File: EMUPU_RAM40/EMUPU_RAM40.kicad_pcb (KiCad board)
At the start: 2 copper layers, 99.1 x 85.2 mm, 29 parts, among them J1 Conn_01x20_Socket, J2 Conn_01x20_Socket, J3 Barrel_Jack_Switch, J4 Conn_01x06_Pin, J5 Conn_01x08_Pin, J7 PinHeader_1x06_P2.54mm_Vertic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, SW1 SW_SPDT, SW2 SW_SPST, U1 PIC18F47Q43-IP, U2 628128

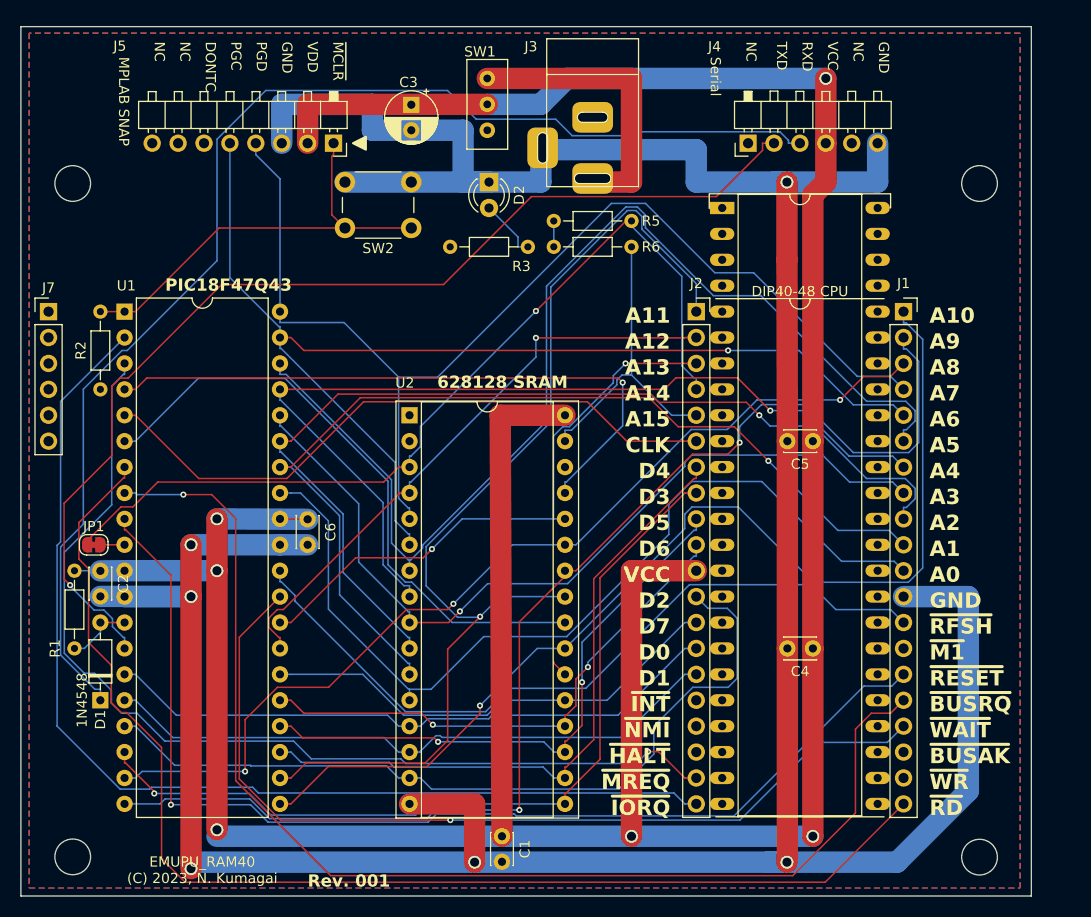
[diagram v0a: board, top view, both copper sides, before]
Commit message: under construction for Rev003 done the follows * fix PowerPlug pin assignment * change /MREQ, /RD, /WR for full_direct * A jumper is assigned to SRAM CS2 (now pulled-up) * add jumpers on /MREQ, /RD, /WR * /INT, /M1 connection to RB5 and RA4. * cut a wire between PB5 and A13, * add pull-down resistors to A13 * add pull up resistors to /MREQ, /RD and /WR.
remains for the following
* add TEST pin
* add LEDs and resistors, including RESET, BUSACK, and HALT
* add pull down resistors to A15-A8, as needed.* add some jumpers for SDcard controls (A9-A12)
* add four jumpers for SDcard (A9-A12)

After confirming 8byte rewrite and reset bootloading, I will finishes the remains.
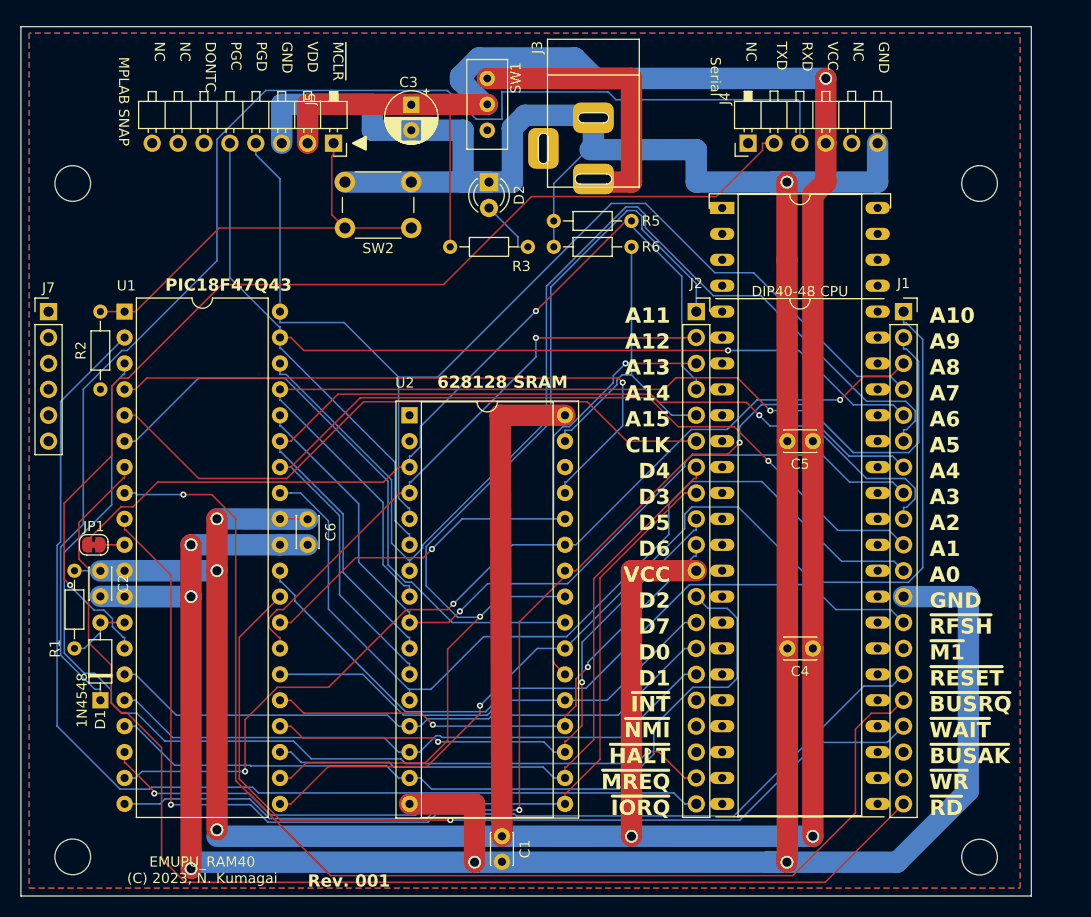
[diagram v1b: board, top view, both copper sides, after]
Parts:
- J3: footprint 0-local:BARREL_JACK -> 0-Project:BARREL_JACK
- J4: footprint 0-local:PinHeader_1x06_P2.54mm_Horizontal_NoFeet -> 0-Project:PinHeader_1x06_P2.54mm_Horizontal_NoFeet
- J5: footprint 0-local:PinHeader_1x08_P2.54mm_Rev_Horizontal_Nofoot -> 0-Project:PinHeader_1x08_P2.54mm_Rev_Horizontal_Nofoot
- SW1: footprint 0-local:PowerSW_for_SBC_series -> 0-Project:PowerSW_for_SBC_series
- SW2: footprint 0-local:SW_PUSH_6mm_H4.3mm -> 0-Project:SW_PUSH_6mm_H4.3mm
- moved J3 0.09 mm to (146.1, 75.0)
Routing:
- net VCC: track 326.7 -> 348.0 mm
- net GND: track 341.8 -> 356.5 mm
- net Net-(D1-K): track 125.3 -> 131.1 mm

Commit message: Rev003: arrange new footprints, before autorouting
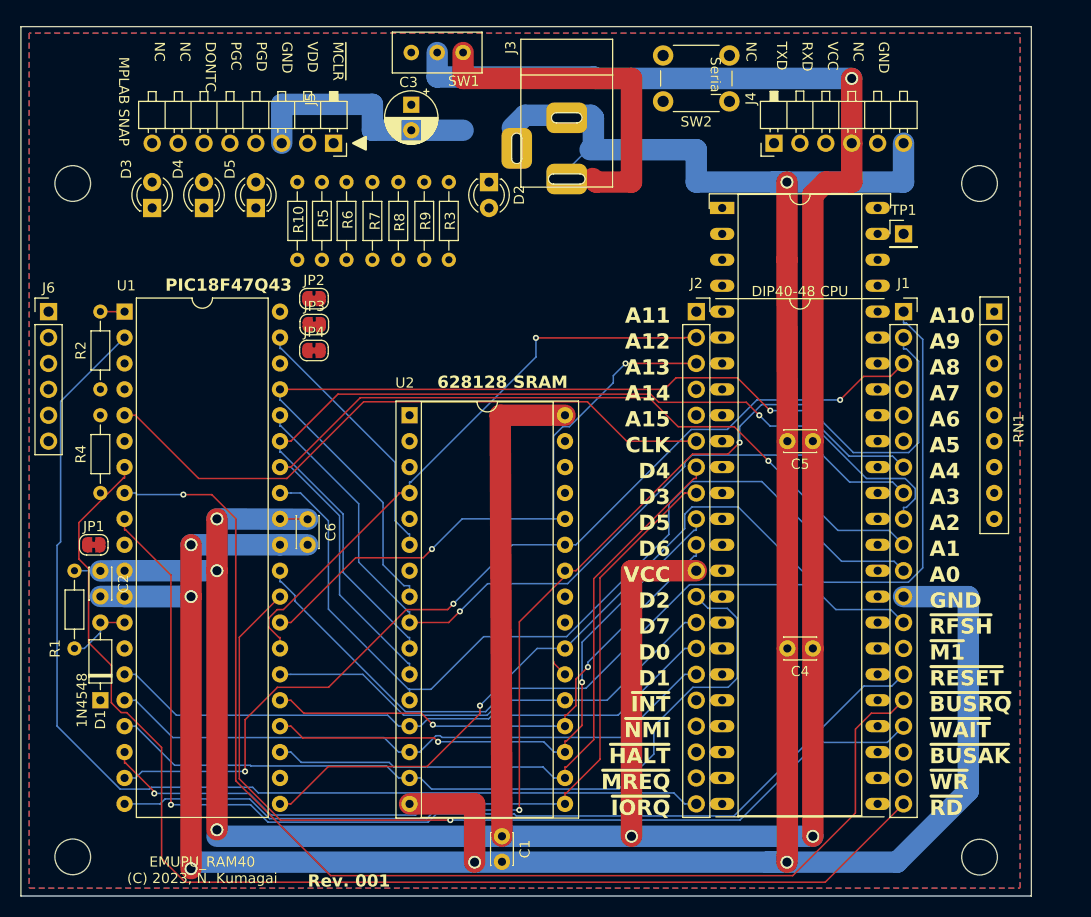
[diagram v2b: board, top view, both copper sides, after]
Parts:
- removed J7: PinHeader_1x06_P2.54mm_Vertical, Connector_PinHeader_2.54mm:PinHeader_1x06_P2.54mm_Vertical
- added D3: BUSAK, LED_THT:LED_D3.0mm, F.Cu at (102.9, 83.8)
- added D4: RESET, LED_THT:LED_D3.0mm, F.Cu at (108.0, 83.8)
- added D5: HALT, LED_THT:LED_D3.0mm, F.Cu at (113.0, 83.8)
- added J6: Conn_01x06_Pin, Connector_PinHeader_2.54mm:PinHeader_1x06_P2.54mm_Vertical, F.Cu at (92.7, 94.0)
- added JP2: SolderJumper_2_Bridged, Jumper:SolderJumper-2_P1.3mm_Bridged_RoundedPad1.0x1.5mm, F.Cu at (118.7, 92.7)
- added JP3: SolderJumper_2_Bridged, Jumper:SolderJumper-2_P1.3mm_Bridged_RoundedPad1.0x1.5mm, F.Cu at (118.8, 95.2)
- added JP4: SolderJumper_2_Bridged, Jumper:SolderJumper-2_P1.3mm_Bridged_RoundedPad1.0x1.5mm, F.Cu at (118.7, 97.8)
- added R10: 1.5k, Resistor_THT:R_Axial_DIN0204_L3.6mm_D1.6mm_P7.62mm_Horizontal, F.Cu at (117.1, 81.3)
- added R4: 10k, Resistor_THT:R_Axial_DIN0204_L3.6mm_D1.6mm_P7.62mm_Horizontal, F.Cu at (97.8, 111.8)
- added R7: 10k, Resistor_THT:R_Axial_DIN0204_L3.6mm_D1.6mm_P7.62mm_Horizontal, F.Cu at (124.5, 81.3)
- added R8: 10k, Resistor_THT:R_Axial_DIN0204_L3.6mm_D1.6mm_P7.62mm_Horizontal, F.Cu at (127.0, 81.3)
- added R9: 10k, Resistor_THT:R_Axial_DIN0204_L3.6mm_D1.6mm_P7.62mm_Horizontal, F.Cu at (129.5, 81.3)
- added RN1: R_Network08, Resistor_THT:R_Array_SIP9, F.Cu at (185.4, 94.0)
- added TP1: TEST, Connector_PinHeader_2.54mm:PinHeader_1x01_P2.54mm_Vertical, F.Cu at (176.5, 86.4)
- R5, R6: value 10k -> 1.5k
- moved SW2 33.6 mm to (159.5, 73.4)
- moved R5 30.6 mm to (119.5, 81.3), turned to -90 degrees
- moved R6 28.7 mm to (121.9, 81.3), turned to -90 degrees
- moved SW1 7.07 mm to (130.8, 68.6), turned to 180 degrees
- moved R3 6.35 mm to (132.0, 81.3), turned to -90 degrees
- moved J3 2.61 mm to (143.5, 75.0)
- moved J4 2.54 mm to (163.8, 77.5)
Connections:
- J2 pad 1: /A11 -> Net-(J2-Pin_1)
- J2 pad 2: /A12 -> Net-(J2-Pin_2)
- J2 pad 3: /A13 -> Net-(J2-Pin_3)
- J2 pad 4: /A14 -> Net-(J2-Pin_4)
- J2 pad 5: /A15 -> Net-(J2-Pin_5)
- JP1 pad 1: /A14 -> Net-(JP1-A)
- JP1 pad 2: Net-(JP1-B) -> VCC
- R5 pad 1: /A14 -> VCC
- R5 pad 2: GND -> Net-(D3-A)
- R6 pad 1: /A15 -> VCC
- R6 pad 2: GND -> Net-(D4-A)
- U1 pad 10: Net-(JP1-B) -> /TEST
- U1 pad 19: /A8 -> /SCLK
- U1 pad 20: /A9 -> /MISO
- U1 pad 21: /A10 -> /MOSI
- U1 pad 22: /A11 -> /SS
- U1 pad 27: /A12 -> unconnected-(U1-RD4-Pad27)
- U1 pad 28: /A13 -> /~{INT}
- U1 pad 6: Net-(U1-RA4) -> /~{M1}
- U1 pad 7: /~{RD} -> Net-(JP2-B)
- U2 pad 2: VCC -> Net-(JP4-A)
- U2 pad 22: VCC -> /~{MREQ}
- U2 pad 24: Net-(U1-RA4) -> Net-(JP2-B)
- U2 pad 25: /A11 -> Net-(J2-Pin_1)
- U2 pad 28: /A13 -> Net-(J2-Pin_3)
- U2 pad 3: /A14 -> Net-(J2-Pin_4)
- U2 pad 30: VCC -> Net-(JP1-A)
- U2 pad 31: /A15 -> Net-(J2-Pin_5)
- U2 pad 4: /A12 -> Net-(J2-Pin_2)
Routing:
- net Net-(D1-K): track 131.1 -> 0.00 mm
- net /A7: track 110.9 -> 0.00 mm
- net /A5: track 110.4 -> 0.00 mm
- net Net-(J4-Pin_2): track 105.9 -> 0.00 mm, vias 1 -> 0
- net /A11: track 105.3 -> 0.00 mm, vias 1 -> 0
- net /~{MREQ}: track 99.6 -> 1.73 mm, vias 1 -> 0
- net /A14: track 87.8 -> 0.00 mm, vias 1 -> 0
- net /A6: track 111.2 -> 25.7 mm, vias 1 -> 0
- net Net-(JP3-B): track 62.7 -> 0.00 mm, vias 1 -> 0
- net Net-(U1-RA4): track 60.4 -> 0.00 mm
- net /A12: track 58.6 -> 0.00 mm, vias 1 -> 0
- net (no net): track 0.00 -> 58.6 mm, vias 0 -> 1
- net /~{INT}: track 0.00 -> 57.6 mm, vias 0 -> 2
- net /A13: track 57.6 -> 0.00 mm, vias 2 -> 0
- net Net-(J5-Pin_1): track 42.8 -> 2.37 mm
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
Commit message: Rev003: autorouting done, no no-connection, but some error/warning remains
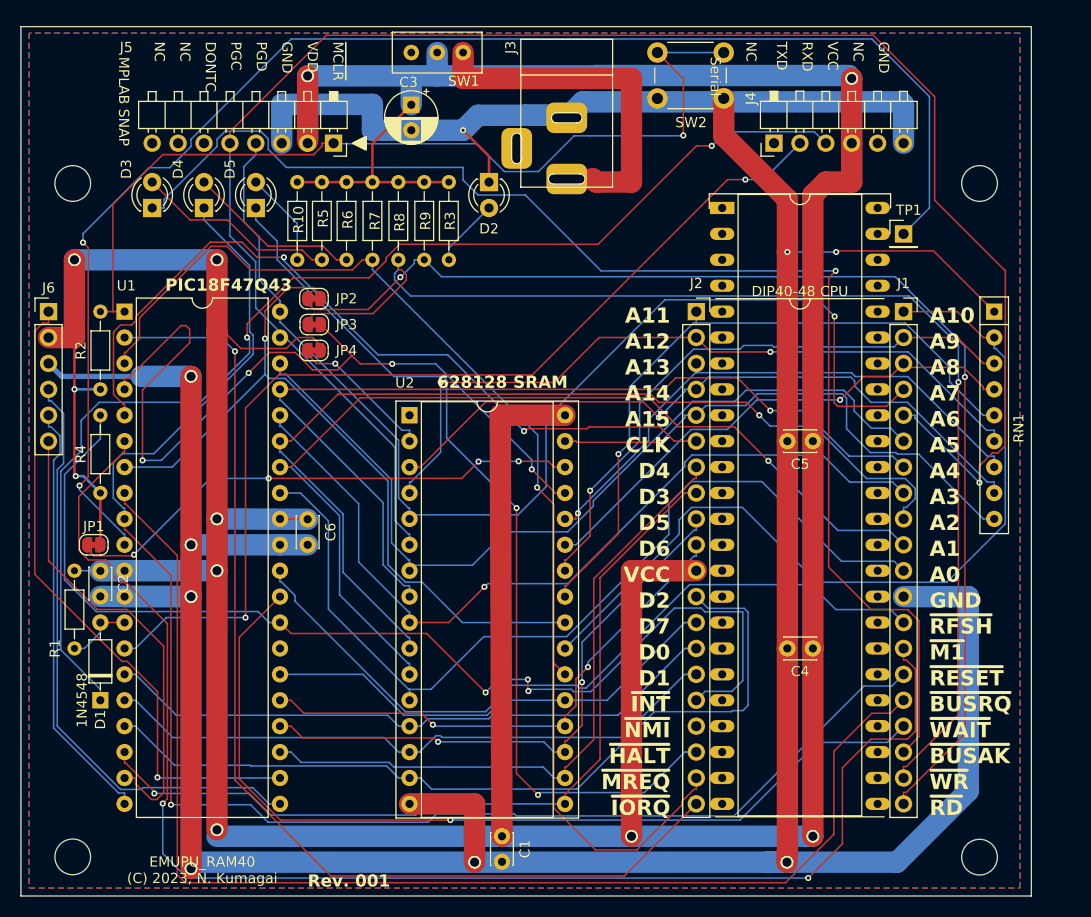
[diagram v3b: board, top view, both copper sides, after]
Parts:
- moved SW2 8.53 mm to (152.4, 68.6), turned to 0 degrees
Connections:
- RN1 pad 2: /A8 -> /A10
- RN1 pad 4: /A10 -> /A8
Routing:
- net /A6: track 25.7 -> 176.4 mm, vias 0 -> 1
- net /~{M1}: track 0.00 -> 141.3 mm, vias 0 -> 2
- net /TEST: track 0.00 -> 141.1 mm, vias 0 -> 2
- net /~{BUSAK}: track 0.00 -> 131.9 mm, vias 0 -> 1
- net VCC: track 315.0 -> 446.8 mm, vias 6 -> 11
- net /~{WR}: track 0.00 -> 119.1 mm, vias 0 -> 1
- net Net-(D1-K): track 0.00 -> 117.2 mm, vias 0 -> 2
- net /A7: track 0.00 -> 115.3 mm, vias 0 -> 1
- net /~{MREQ}: track 1.73 -> 114.4 mm, vias 0 -> 1
- net Net-(J4-Pin_2): track 0.00 -> 98.8 mm, vias 0 -> 2
- net /~{HALT}: track 0.00 -> 89.1 mm, vias 0 -> 2
- net Net-(J5-Pin_1): track 2.37 -> 89.7 mm, vias 0 -> 1
- net /A5: track 0.00 -> 84.5 mm
- net Net-(JP3-B): track 0.00 -> 82.1 mm, vias 0 -> 4
- net Net-(JP2-B): track 0.00 -> 75.1 mm, vias 0 -> 1
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
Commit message: Rev003: ordered to JLCPCB
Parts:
- removed DIP40-48 CPU: DIP-48_W15.24mm_Socket_OvalPad_nocourtyard, 0-local:DIP-48_W15.24mm_Socket_OvalPad_splitcouryard
- added U10: DIP-48_W15.24mm_Socket_OvalPad_nocourtyard, 0-Project:DIP-48_W15.24mm_Socket_OvalPad_splitcouryard, F.Cu at (158.8, 83.8)
- moved R4 20.7 mm to (95.5, 91.2), turned to 0 degrees
- moved R2 13.2 mm to (95.5, 88.6), turned to 0 degrees
- moved R5 2.54 mm to (122.0, 81.3)
- moved R6 2.29 mm to (119.6, 81.3)
- turned JP1 to 180 degrees
- turned JP4 to 180 degrees
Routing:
- net VCC: track 446.8 -> 430.2 mm, vias 11 -> 9
- net Net-(JP1-A): track 51.6 -> 68.1 mm, vias 4 -> 3
- net /~{MREQ}: track 114.4 -> 129.6 mm
- net Net-(JP3-B): track 82.1 -> 68.7 mm
- net /CLK: track 78.3 -> 66.7 mm
- net /~{INT}: track 106.1 -> 116.4 mm, vias 3 -> 4
- net /~{RESET}: track 149.2 -> 142.8 mm, vias 1 -> 2
- net /A4: track 91.2 -> 97.1 mm
- net Net-(D3-A): track 19.8 -> 24.6 mm
- net /~{M1}: track 141.3 -> 137.6 mm
- net /A1: track 96.2 -> 98.6 mm
- net /~{RFSH}: track 74.7 -> 77.0 mm
- net /A7: track 115.3 -> 117.5 mm
- net /A2: track 97.4 -> 99.2 mm
- net Net-(J2-Pin_2): track 73.1 -> 74.5 mm
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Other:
- board text added: "MISO"
- board text added: "MOSI"
- board text added: "Rev. 003 (DIRECT)"
- board text added: "SCLK"
- board text added: "SDcard"
- board text added: "SS"
- board text removed: "Rev. 001"

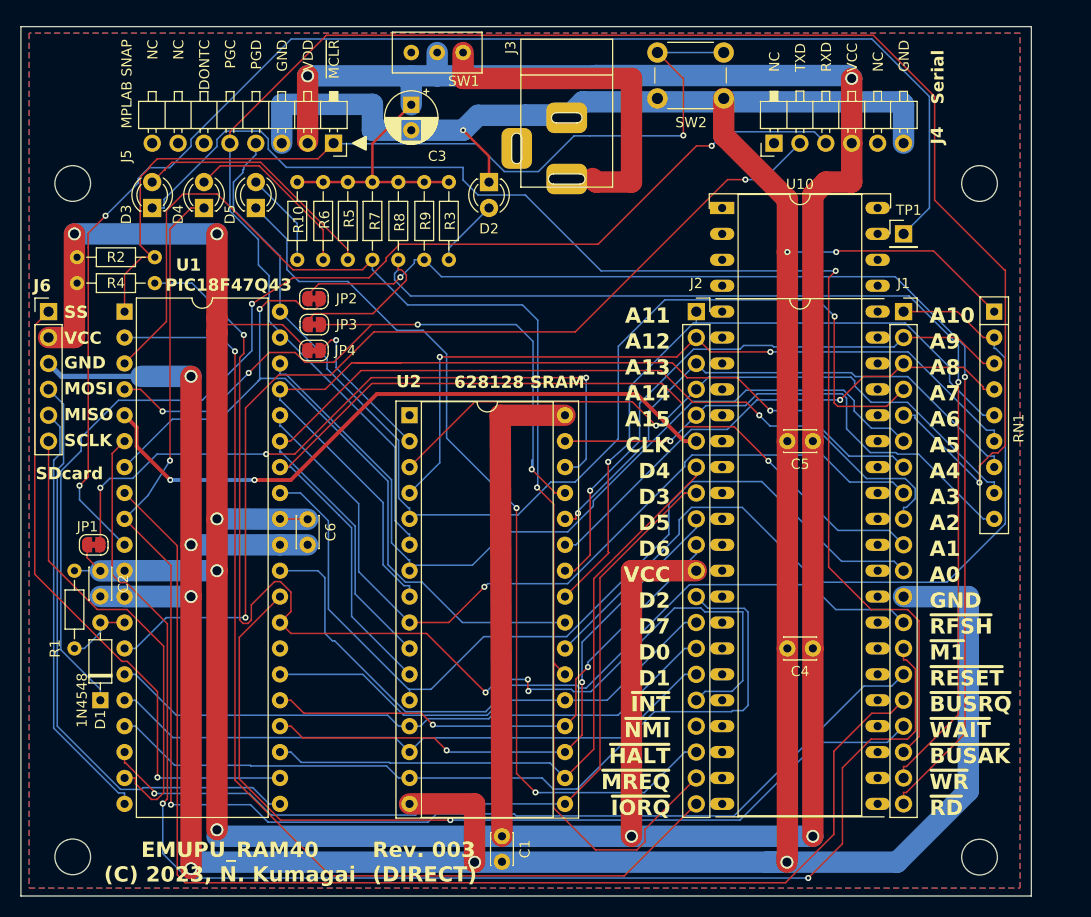
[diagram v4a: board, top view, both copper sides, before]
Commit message: Rev004, add 10k pullup resister to IORQ
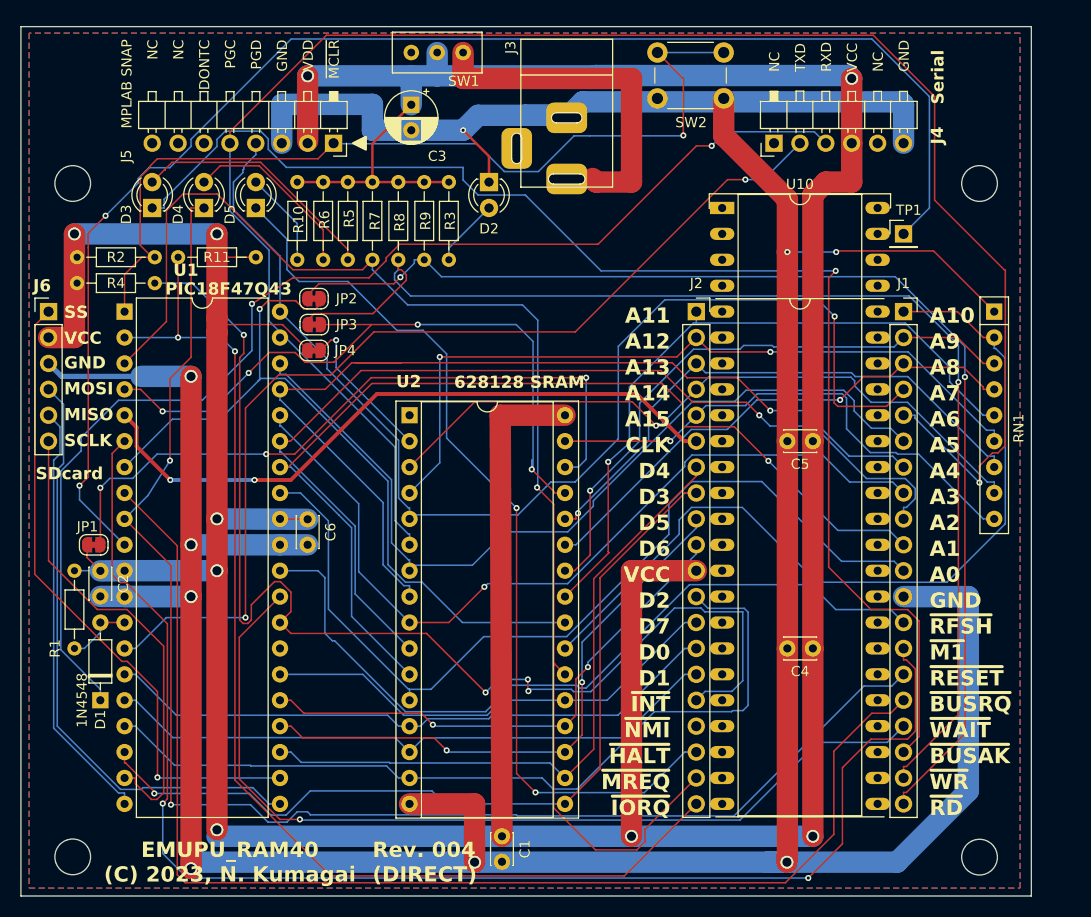
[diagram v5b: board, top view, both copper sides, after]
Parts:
- added R11: 10k, Resistor_THT:R_Axial_DIN0204_L3.6mm_D1.6mm_P7.62mm_Horizontal, F.Cu at (113.0, 88.6)
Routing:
- net /~{IORQ}: track 105.5 -> 113.3 mm, vias 1 -> 2
- net VCC: track 430.2 -> 434.1 mm
- net /D3: track 83.4 -> 84.4 mm
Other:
- board text added: "Rev. 004 (DIRECT)"
- board text removed: "Rev. 003 (DIRECT)"
